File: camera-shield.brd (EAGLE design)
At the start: 58.8 x 25.4 mm, 21 parts, among them T1 TG110-S055N2RL

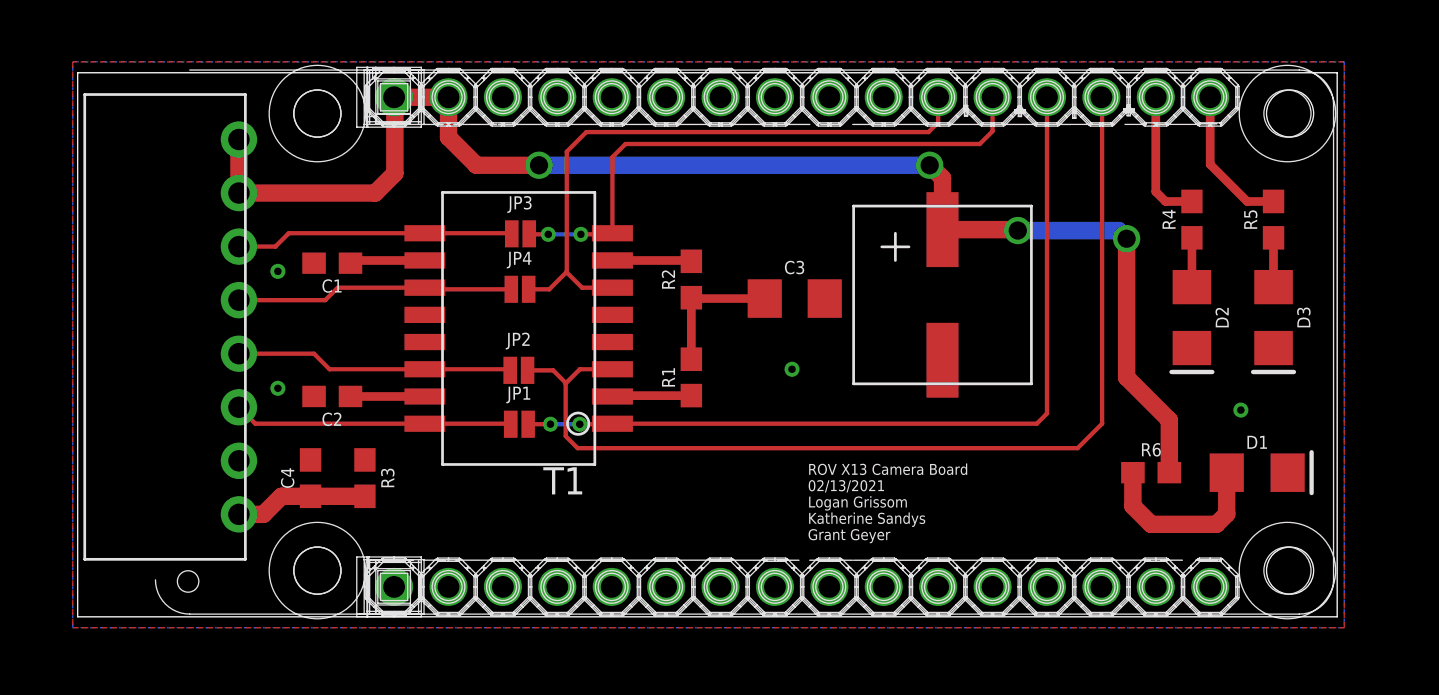
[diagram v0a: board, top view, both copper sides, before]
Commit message: Flip ethernet termination, use transformer symbol, clean up repo a little
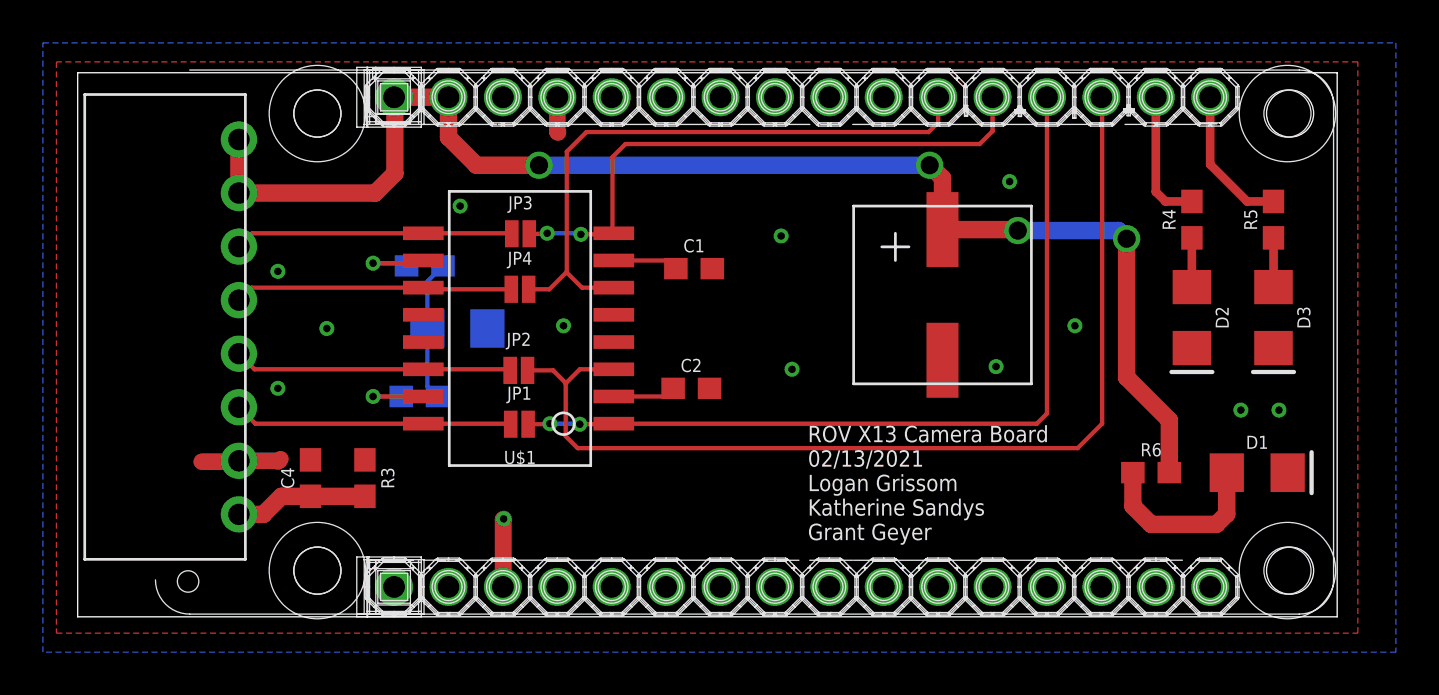
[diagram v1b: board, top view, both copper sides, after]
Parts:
- removed T1: TG110-S055N2RL, CameraBoard_Library:TG110-S055N2RL
- added U$1: ETH-TRANS, ethernet transformer:SOIC-16-WIDE
- moved C1 16.9 mm to (34.5, 16.3), turned to 0 degrees
- moved C2 16.8 mm to (34.4, 10.7), turned to 0 degrees
- moved C3 15.8 mm to (23.5, 13.5), flipped to the bottom, turned to 180 degrees
- moved R1 12.7 mm to (21.7, 10.3), flipped to the bottom, turned to 180 degrees
- moved R2 12.5 mm to (22.0, 16.4), flipped to the bottom, turned to 0 degrees
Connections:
- net ETH_RD_N: now also U$1.6; no longer T1.6
- net ETH_RD_P: now also U$1.8; no longer T1.8
- net ETH_TD0_GND: now also U$1.7; no longer T1.10
- net ETH_TD1_GND: now also U$1.2; no longer T1.15
- net ETH_TD_N: now also U$1.1; no longer T1.1
- net ETH_TD_P: now also U$1.3; no longer T1.3
- net GND: now also U$2.GND_2
- net N$11: now also U$1.15; no longer T1.2
- net N$3: now also U$1.10; no longer T1.7
- net RD_N: now also U$1.11; no longer T1.11
- net RD_P: now also U$1.9; no longer T1.9
- net TD_N: now also U$1.16; no longer T1.16
- net TD_P: now also U$1.14; no longer T1.14
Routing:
- net GND: track 0.00 -> 17.0 mm, vias 4 -> 13
- net ETH_TD1_GND: track 3.47 -> 2.93 mm
- net N$3: track 3.70 -> 4.02 mm, vias 0 -> 1
- net N$11: track 3.70 -> 3.66 mm, vias 0 -> 1
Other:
- board text added: "TD- TD+ RD- RD+"
